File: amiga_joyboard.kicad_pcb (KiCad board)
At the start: 2 copper layers, 192.5 x 63.5 mm, 27 parts, among them J1 JOYPORT_OUT, J2 CONN_D, J3 CONN_F, SW1 FIRE_BTN, SW2 B_BTN, SW3 A_BTN, SW4 RIGHT_BTN, SW5 LEFT_BTN, SW6 DOWN_BTN, SW7 UP_BTN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

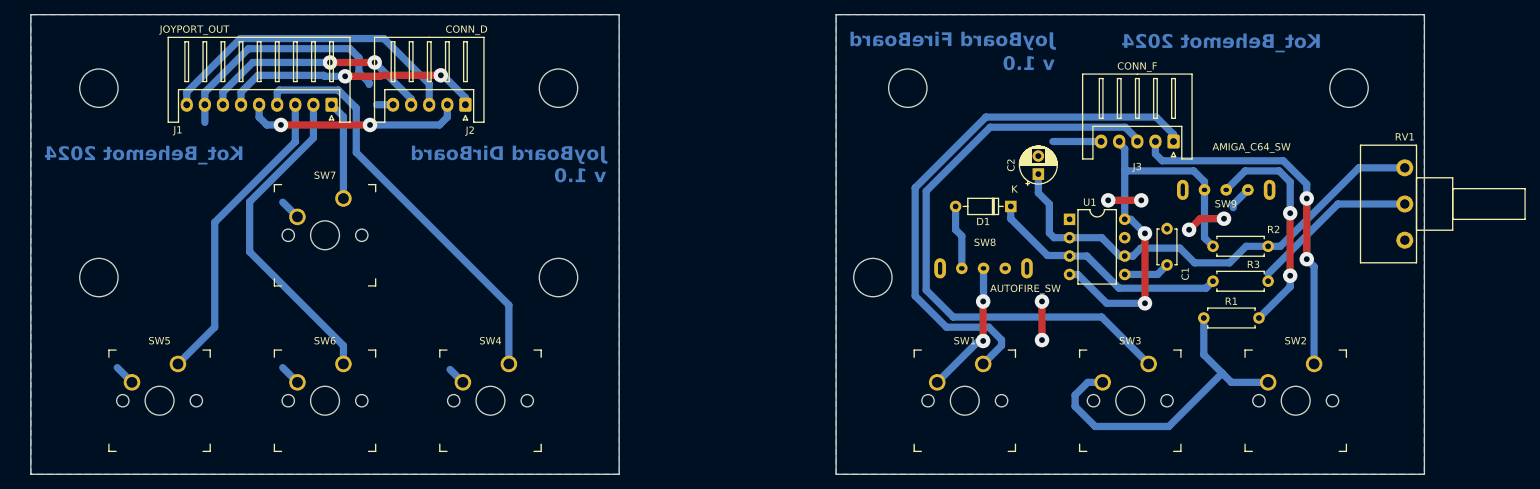
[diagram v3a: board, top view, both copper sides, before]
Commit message: more button movement
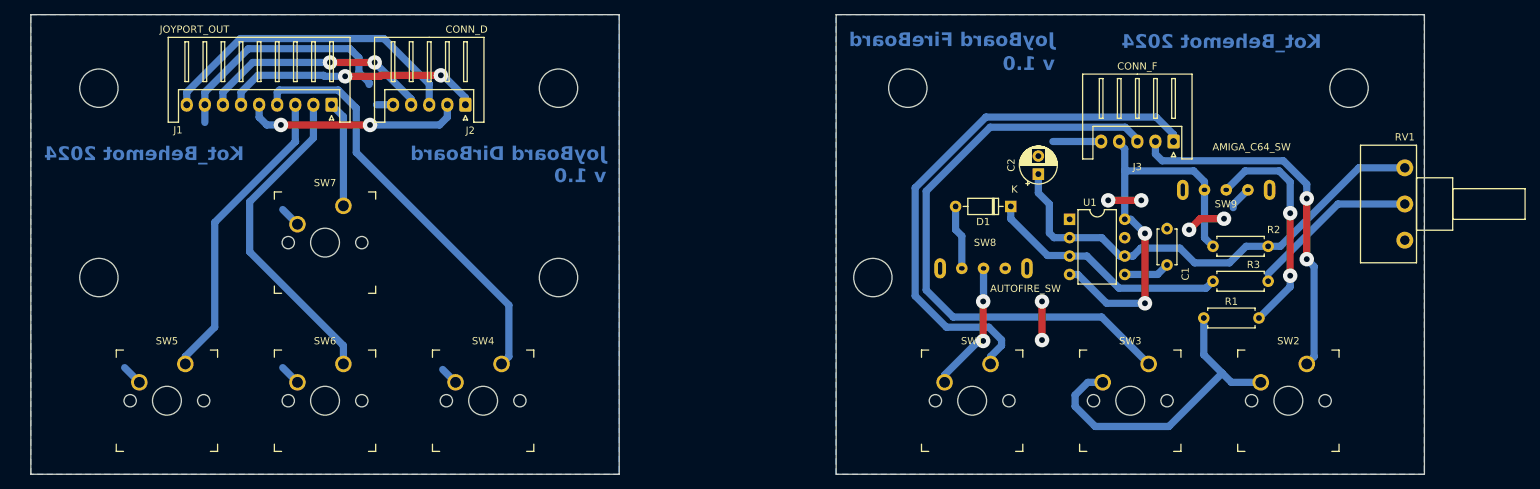
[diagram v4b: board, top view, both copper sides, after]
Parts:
- moved SW4 1.02 mm to (111.5, 118.6)
- moved SW7 1.02 mm to (89.7, 96.8)
- moved SW1 1.02 mm to (179.1, 118.6)
- moved SW2 1.02 mm to (222.8, 118.6)
- moved SW5 1.02 mm to (67.8, 118.6)
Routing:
- net /UP: track 13.6 -> 14.7 mm
- net Net-(R1-Pad1): track 46.2 -> 45.2 mm
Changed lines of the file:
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@@
 	(footprint "Amiga Joyboard:SW_MX"
 		(layer "F.Cu")
-		(at 66.802 118.618)
+		(at 67.818 118.618)
 		(descr "MX-style keyswitch")
 		(tags "MX,cherry,gateron,kailh")
@@
 	(footprint "Amiga Joyboard:SW_MX"
 		(layer "F.Cu")
-		(at 178.054 118.618)
+		(at 179.07 118.618)
 		(descr "MX-style keyswitch")
 		(tags "MX,cherry,gateron,kailh")
@@
 	(footprint "Amiga Joyboard:SW_MX"
 		(layer "F.Cu")
-		(at 89.662 95.758)
+		(at 89.662 96.774)
 		(descr "MX-style keyswitch")
 		(tags "MX,cherry,gateron,kailh")
@@
 	(footprint "Amiga Joyboard:SW_MX"
 		(layer "F.Cu")
-		(at 223.774 118.618)
+		(at 222.758 118.618)
 		(descr "MX-style keyswitch")
 		(tags "MX,cherry,gateron,kailh")
@@
 	(footprint "Amiga Joyboard:SW_MX"
 		(layer "F.Cu")
-		(at 112.522 118.618)
+		(at 111.506 118.618)
 		(descr "MX-style keyswitch")
 		(tags "MX,cherry,gateron,kailh")
@@
 	)
 	(segment
-		(start 108.712 116.078)
-		(end 106.934 114.3)
-		(width 1)
-		(layer "B.Cu")
-		(net 9)
-	)
-	(segment
-		(start 85.852 93.218)
-		(end 83.82 91.186)
+		(start 64.008 116.078)
+		(end 61.976 114.046)
 		(width 1)
 		(layer "B.Cu")
@@
 	)
 	(segment
+		(start 85.852 94.234)
+		(end 83.82 92.202)
+		(width 1)
+		(layer "B.Cu")
+		(net 9)
+	)
+	(segment
 		(start 93.094 69.98)
 		(end 93.472 70.358)
@@
 	)
 	(segment
-		(start 62.992 116.078)
-		(end 60.96 114.046)
+		(start 107.696 116.078)
+		(end 105.918 114.3)
 		(width 1)
 		(layer "B.Cu")
@@
 	)
 	(segment
-		(start 83.365 75.692)
-		(end 91.484274 75.692)
+		(start 83.058 77.724)
+		(end 83.058 75.999)
 		(width 1)
 		(layer "B.Cu")
@@
 	)
 	(segment
-		(start 115.062 105.41)
-		(end 115.062 113.538)
+		(start 83.058 75.999)
+		(end 83.365 75.692)
 		(width 1)
 		(layer "B.Cu")
@@
 	)
 	(segment
-		(start 91.484274 75.692)
-		(end 93.98 78.187726)
+		(start 93.98 84.328)
+		(end 115.062 105.41)
 		(width 1)
 		(layer "B.Cu")
@@
 	)
 	(segment
-		(start 83.058 75.999)
-		(end 83.365 75.692)
+		(start 83.365 75.692)
+		(end 91.484274 75.692)
 		(width 1)
 		(layer "B.Cu")
@@
 	)
 	(segment
-		(start 93.98 84.328)
-		(end 115.062 105.41)
+		(start 91.484274 75.692)
+		(end 93.98 78.187726)
 		(width 1)
 		(layer "B.Cu")
@@
 	)
 	(segment
-		(start 83.058 77.724)
-		(end 83.058 75.999)
+		(start 115.062 112.522)
+		(end 114.046 113.538)
 		(width 1)
 		(layer "B.Cu")
@@
 	)
 	(segment
+		(start 115.062 105.41)
+		(end 115.062 112.522)
+		(width 1)
+		(layer "B.Cu")
+		(net 10)
+	)
+	(segment
 		(start 70.558 77.724)
 		(end 70.558 75.999)
@@
 	)
 	(segment
-		(start 74.422 108.458)
-		(end 69.342 113.538)
+		(start 85.558 82.764)
+		(end 85.598 82.804)
 		(width 1)
 		(layer "B.Cu")
@@
 	)
 	(segment
-		(start 74.422 93.98)
-		(end 85.598 82.804)
+		(start 70.358 112.522)
+		(end 70.358 113.538)
+		(width 1)
+		(layer "B.Cu")
+		(net 12)
+	)
+	(segment
+		(start 74.422 108.458)
+		(end 70.358 112.522)
 		(width 1)
 		(layer "B.Cu")
@@
 	)
 	(segment
-		(start 85.558 82.764)
-		(end 85.558 77.724)
+		(start 85.598 82.804)
+		(end 74.422 93.98)
 		(width 1)
 		(layer "B.Cu")
@@
 	)
 	(segment
-		(start 85.598 82.804)
+		(start 85.558 77.724)
 		(end 85.558 82.764)
 		(width 1)
@@
 	)
 	(segment
-		(start 90.558 77.724)
-		(end 92.202 79.368)
+		(start 92.202 79.368)
+		(end 92.202 91.694)
 		(width 1)
 		(layer "B.Cu")
@@
 	)
 	(segment
-		(start 92.202 79.368)
-		(end 92.202 90.678)
+		(start 90.558 77.724)
+		(end 92.202 79.368)
 		(width 1)
 		(layer "B.Cu")
@@
 	)
 	(segment
+		(start 214.884 116.078)
+		(end 218.948 116.078)
+		(width 1)
+		(layer "B.Cu")
+		(net 15)
+	)
+	(segment
 		(start 196.065325 122.174)
 		(end 206.248 122.174)
@@
 	)
 	(segment
-		(start 214.884 116.078)
-		(end 219.964 116.078)
-		(width 1)
-		(layer "B.Cu")
-		(net 15)
-	)
-	(segment
 		(start 193.294 117.833325)
 		(end 193.294 119.402675)
@@
 	)
 	(segment
-		(start 179.964 110.358)
-		(end 174.244 116.078)
+		(start 175.26 115.062)
+		(end 175.26 116.078)
 		(width 1)
 		(layer "B.Cu")
@@
 	)
 	(segment
-		(start 180.594 110.358)
-		(end 179.964 110.358)
+		(start 180.642 104.854)
+		(end 180.594 104.902)
 		(width 1)
 		(layer "B.Cu")
@@
 	)
 	(segment
-		(start 180.642 104.854)
-		(end 180.594 104.902)
+		(start 179.964 110.358)
+		(end 175.26 115.062)
+		(width 1)
+		(layer "B.Cu")
+		(net 18)
+	)
+	(segment
+		(start 180.594 110.358)
+		(end 179.964 110.358)
 		(width 1)
 		(layer "B.Cu")
@@
 	)
 	(segment
+		(start 226.314 100.076)
+		(end 226.314 112.522)
+		(width 1)
+		(layer "B.Cu")
+		(net 22)
+	)
+	(segment
 		(start 204.39 82.804)
 		(end 204.39 84.529)
@@
 	)
 	(segment
-		(start 225.298 99.06)
-		(end 226.314 100.076)
+		(start 226.314 112.522)
+		(end 225.298 113.538)
 		(width 1)
 		(layer "B.Cu")
@@
 	)
 	(segment
-		(start 226.314 100.076)
-		(end 226.314 113.538)
+		(start 204.39 84.529)
+		(end 205.329 85.468)
 		(width 1)
 		(layer "B.Cu")
@@
 	)
 	(segment
-		(start 204.39 84.529)
-		(end 205.329 85.468)
+		(start 225.298 99.06)
+		(end 226.314 100.076)
 		(width 1)
 		(layer "B.Cu")
@@
 	)
 	(segment
-		(start 183.134 110.210994)
-		(end 183.134 110.998)
+		(start 175.514 108.458)
+		(end 181.381006 108.458)
 		(width 1)
 		(layer "B.Cu")
@@
 	)
 	(segment
-		(start 183.134 110.998)
-		(end 180.594 113.538)
+		(start 181.61 112.522)
+		(end 181.61 113.538)
 		(width 1)
 		(layer "B.Cu")
@@
 	)
 	(segment
-		(start 171.196 104.14)
-		(end 175.514 108.458)
+		(start 183.134 110.210994)
+		(end 183.134 110.998)
 		(width 1)
 		(layer "B.Cu")
@@
 	)
 	(segment
+		(start 204.49 79.429)
+		(end 180.973101 79.429)
+		(width 1)
+		(layer "B.Cu")
+		(net 24)
+	)
+	(segment
 		(start 171.196 89.206101)
 		(end 171.196 104.14)
@@
 	)
 	(segment
-		(start 206.89 82.804)
-		(end 206.89 81.829)
+		(start 171.196 104.14)
+		(end 175.514 108.458)
 		(width 1)
 		(layer "B.Cu")
@@
 	)
 	(segment
-		(start 175.514 108.458)
-		(end 181.381006 108.458)
+		(start 183.134 110.998)
+		(end 181.61 112.522)
 		(width 1)
 		(layer "B.Cu")
@@
 	)
 	(segment
-		(start 204.49 79.429)
-		(end 180.973101 79.429)
+		(start 206.89 81.829)
+		(end 204.49 79.429)
 		(width 1)
 		(layer "B.Cu")
@@
 	)
 	(segment
-		(start 206.89 81.829)
-		(end 204.49 79.429)
+		(start 206.89 82.804)
+		(end 206.89 81.829)
 		(width 1)
 		(layer "B.Cu")
